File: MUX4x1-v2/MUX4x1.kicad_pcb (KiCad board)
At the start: 2 copper layers, 85.1 x 50.8 mm, 14 parts, among them J1 Screw_Terminal_01x02, J2 Conn_01x09_Male, J3 Conn_01x09_Male, J4 Conn_01x09_Male, J5 Conn_01x09_Male, J6 Conn_01x09_Male, J7 Conn_01x03_Male, U1 74LS153, U2 74LS153, U3 74LS153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

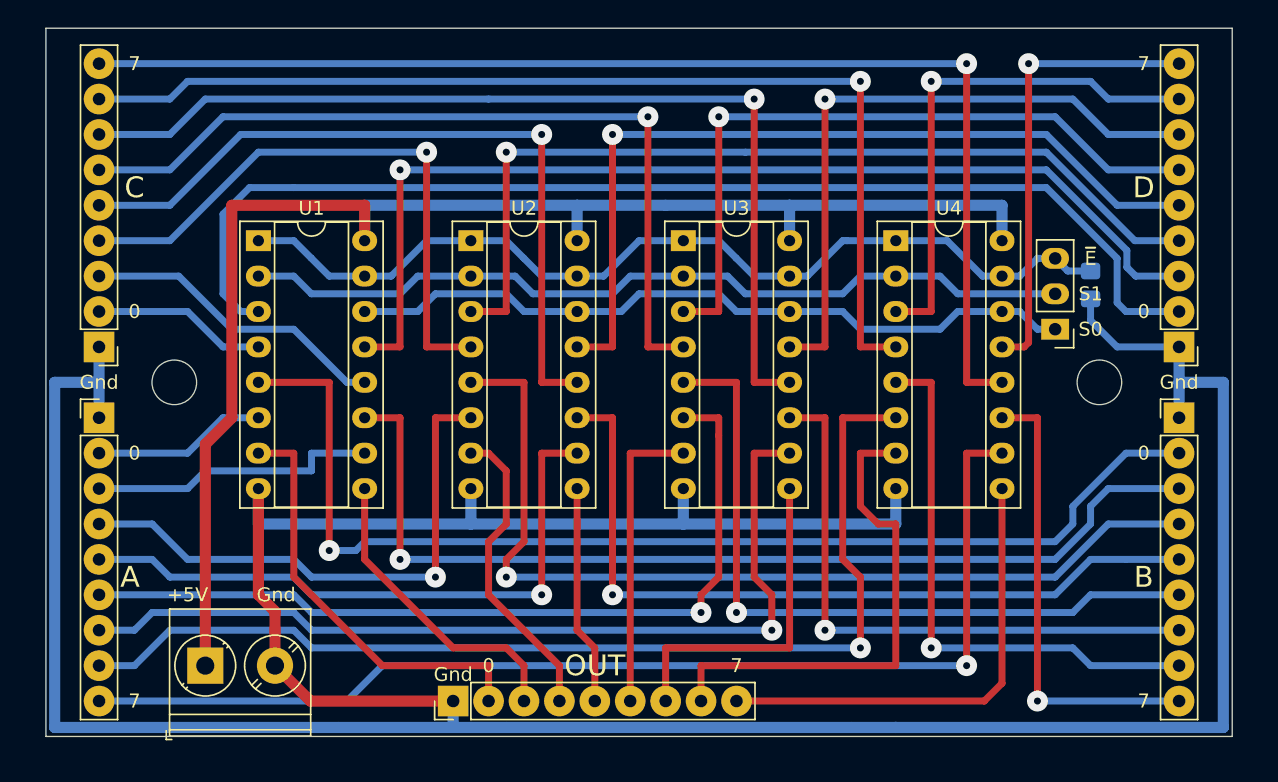
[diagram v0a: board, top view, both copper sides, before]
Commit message: We need more sockets!!
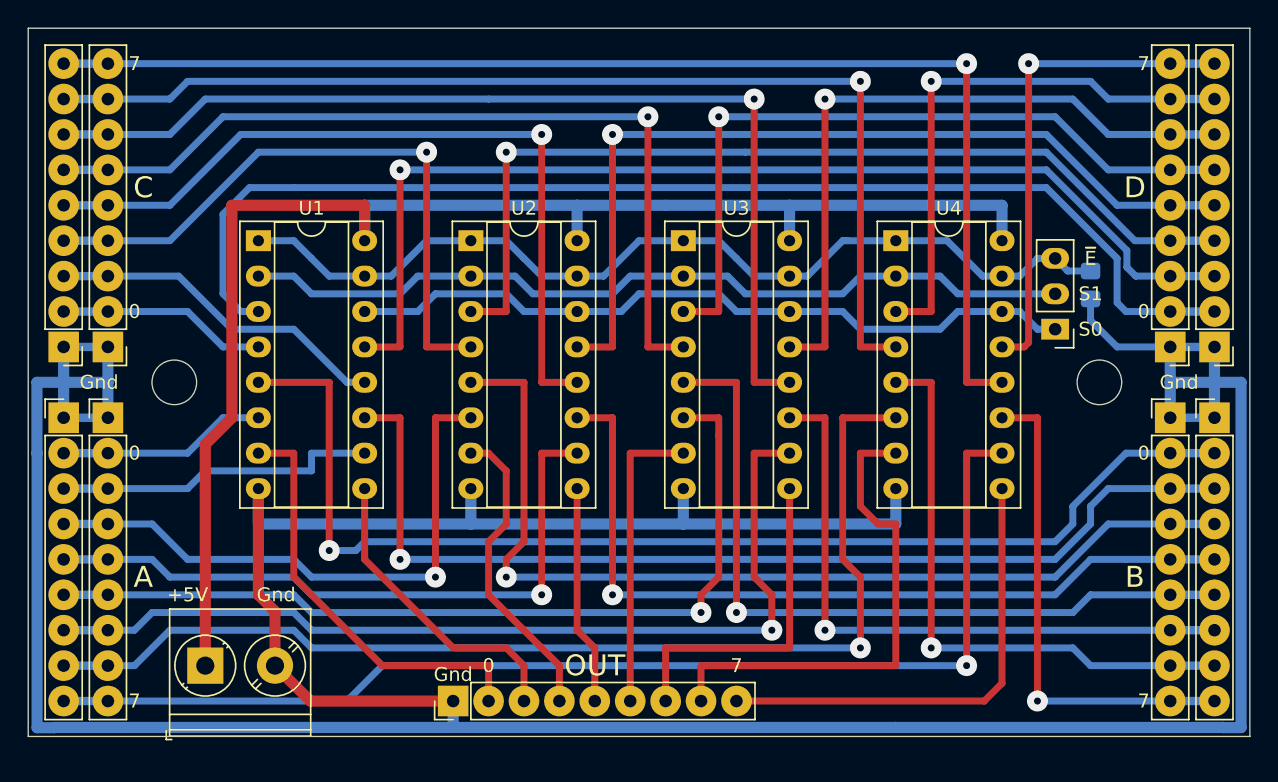
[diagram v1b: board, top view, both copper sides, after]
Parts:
- added J10: Conn_01x09_Male, Connector_PinHeader_2.54mm:PinHeader_1x09_P2.54mm_Vertical, F.Cu at (73.7, 81.3)
- added J11: Conn_01x09_Male, Connector_PinHeader_2.54mm:PinHeader_1x09_P2.54mm_Vertical, F.Cu at (156.2, 81.3)
- added J8: Conn_01x09_Male, Connector_PinHeader_2.54mm:PinHeader_1x09_P2.54mm_Vertical, F.Cu at (73.7, 86.4)
- added J9: Conn_01x09_Male, Connector_PinHeader_2.54mm:PinHeader_1x09_P2.54mm_Vertical, F.Cu at (156.2, 86.4)
- moved J2 0.63 mm to (76.8, 86.4)
- moved J3 0.63 mm to (153.0, 86.4)
- moved J4 0.63 mm to (76.8, 81.3)
- moved J5 0.63 mm to (153.0, 81.3)
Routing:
- net GND: track 243.3 -> 272.6 mm
- net /D7: track 32.8 -> 35.9 mm
- net /D6: track 37.4 -> 40.5 mm
- net /D5: track 46.8 -> 49.9 mm
- net /D4: track 51.1 -> 54.3 mm
- net /D3: track 60.5 -> 63.7 mm
- net /D2: track 64.9 -> 68.0 mm
- net /D1: track 75.0 -> 78.2 mm
- net /D0: track 83.7 -> 86.9 mm
- net /C6: track 76.7 -> 79.9 mm
- net /C5: track 70.9 -> 74.1 mm
- net /B7: track 33.0 -> 36.2 mm
- net /B6: track 39.9 -> 43.1 mm
- net /B5: track 43.2 -> 46.4 mm
- net /B4: track 52.6 -> 55.8 mm
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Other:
- board size 85.1 x 50.8 mm -> 87.6 x 50.8 mm

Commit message: Add date & photomask
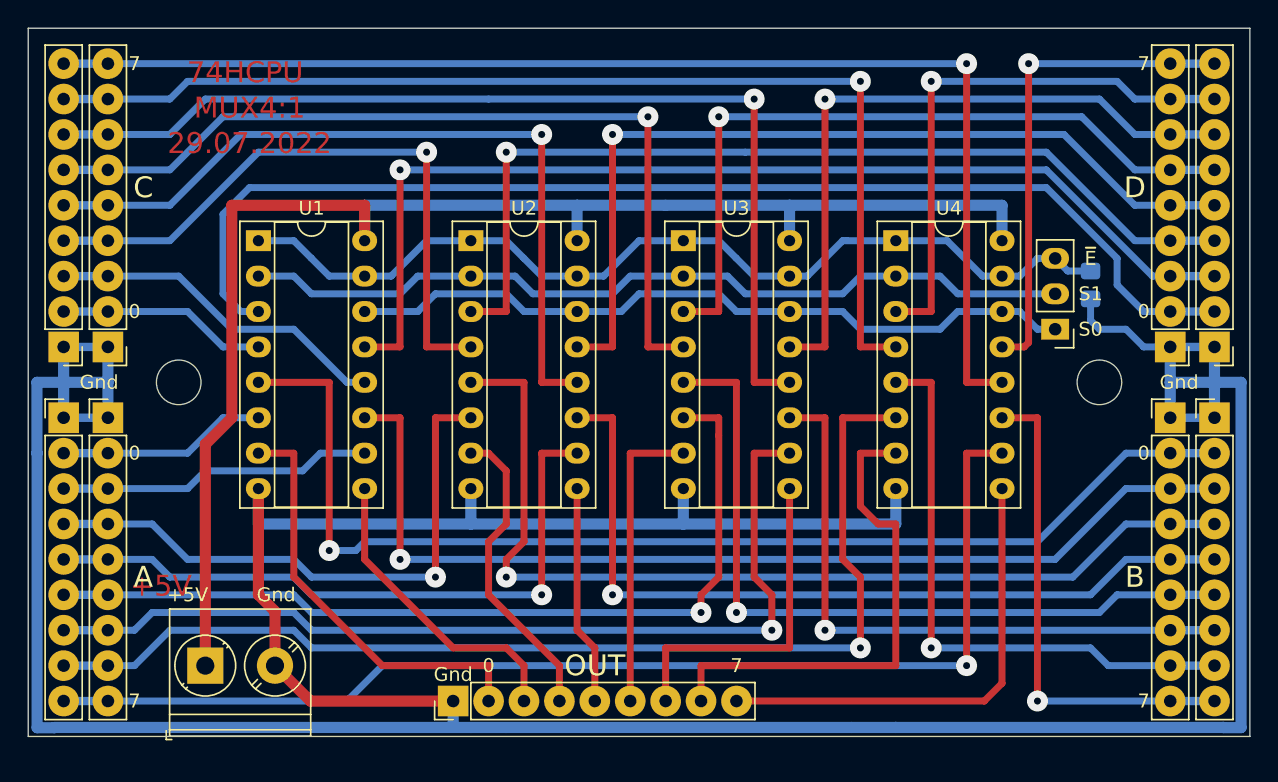
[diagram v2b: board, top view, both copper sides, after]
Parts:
- moved H1 0.32 mm to (81.9, 83.8)
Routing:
- net /B1: track 74.6 -> 73.9 mm
- net /A1: track 24.0 -> 23.3 mm
- net /D0: track 86.9 -> 86.1 mm
- net /B0: track 84.9 -> 84.2 mm
- net /D1: track 78.2 -> 77.5 mm
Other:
- board text added: "29.07.2022"
- board text added: "74HCPU"
- board text added: "MUX4:1"

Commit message: MUX4:1 - we need more rivets!!
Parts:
- moved H2 21.7 mm to (146.1, 105.4)
- moved H1 21.7 mm to (83.8, 62.2)
- moved J1 0.90 mm to (83.2, 104.8)
- moved J7 0.64 mm to (144.8, 79.4)
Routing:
- net /C7: track 90.8 -> 94.5 mm, vias 1 -> 2
- net /B5: track 46.4 -> 49.0 mm, vias 1 -> 2
- net /A7: track 84.2 -> 86.8 mm, vias 1 -> 2
- net /B6: track 43.1 -> 45.3 mm, vias 1 -> 2
- net /B7: track 36.2 -> 34.0 mm, vias 1 -> 2
- net /C6: track 79.9 -> 82.0 mm, vias 1 -> 2
- net /B2: track 71.3 -> 69.5 mm, vias 1 -> 2
- net /B0: track 84.2 -> 82.7 mm, vias 1 -> 2
- net GND: track 272.6 -> 271.5 mm
- net /~E: track 68.0 -> 69.0 mm
- net /A5: track 68.3 -> 69.3 mm, vias 1 -> 2
- net /C5: track 74.1 -> 75.1 mm, vias 1 -> 2
- net /B4: track 55.8 -> 56.7 mm, vias 1 -> 2
- net VCC: track 101.8 -> 102.7 mm
- net /O5: track 24.1 -> 24.9 mm
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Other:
- board text added: "31.07.2022"
- board text removed: "29.07.2022"

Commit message: MUX 4:1 PCB is ready
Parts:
- added D1: LED, LED_SMD:LED_0805_2012Metric_Pad1.15x1.40mm_HandSolder, F.Cu at (146.1, 97.8)
- added D2: LED, LED_SMD:LED_0805_2012Metric_Pad1.15x1.40mm_HandSolder, F.Cu at (148.6, 97.8)
- added R2: 1k, Resistor_SMD:R_0805_2012Metric_Pad1.20x1.40mm_HandSolder, F.Cu at (146.1, 92.7)
- added R3: 1k, Resistor_SMD:R_0805_2012Metric_Pad1.20x1.40mm_HandSolder, F.Cu at (148.6, 92.7)
- R1: value R -> 10k
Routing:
- net GND: track 271.5 -> 291.0 mm
- net /S1: track 61.1 -> 79.9 mm
- net /S0: track 52.9 -> 68.0 mm
- net Net-(D2-Pad2): track 0.00 -> 3.06 mm
- net Net-(D1-Pad2): track 0.00 -> 3.06 mm
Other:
- board text added: "09.10.2022"
- board text removed: "31.07.2022"

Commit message: Polishing MUX4:1
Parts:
- added J12: Conn_01x09_Male, Connector_PinHeader_2.54mm:PinHeader_1x09_P2.54mm_Vertical, F.Cu at (101.6, 108.9)
- moved J6 0.64 mm to (101.6, 106.0)
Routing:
- net GND: track 291.0 -> 295.3 mm, vias 0 -> 1
- net /O6: track 35.9 -> 39.1 mm
- net /O7: track 33.5 -> 36.7 mm
- net /O4: track 21.2 -> 24.1 mm
- net /O3: track 15.8 -> 18.6 mm
- net /O2: track 22.1 -> 24.9 mm
- net /O1: track 22.2 -> 25.1 mm
- net /O0: track 29.8 -> 32.7 mm
- net /O5: track 24.9 -> 26.7 mm
- net /B5: track 49.0 -> 47.9 mm
- net /A5: track 69.3 -> 68.5 mm
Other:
- board size 87.6 x 50.8 mm -> 87.6 x 52.1 mm
- board text added: "02.11.2022"
- board text added: "1"
- board text removed: "09.10.2022"
